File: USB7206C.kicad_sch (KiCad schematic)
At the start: 38 parts, among them J1 USB_SPI_(Opt), SW1 RESET_HUB, U2 MIC803-29D4VM3-TR, U27 USB7206C/KDX, Y1 25MHz

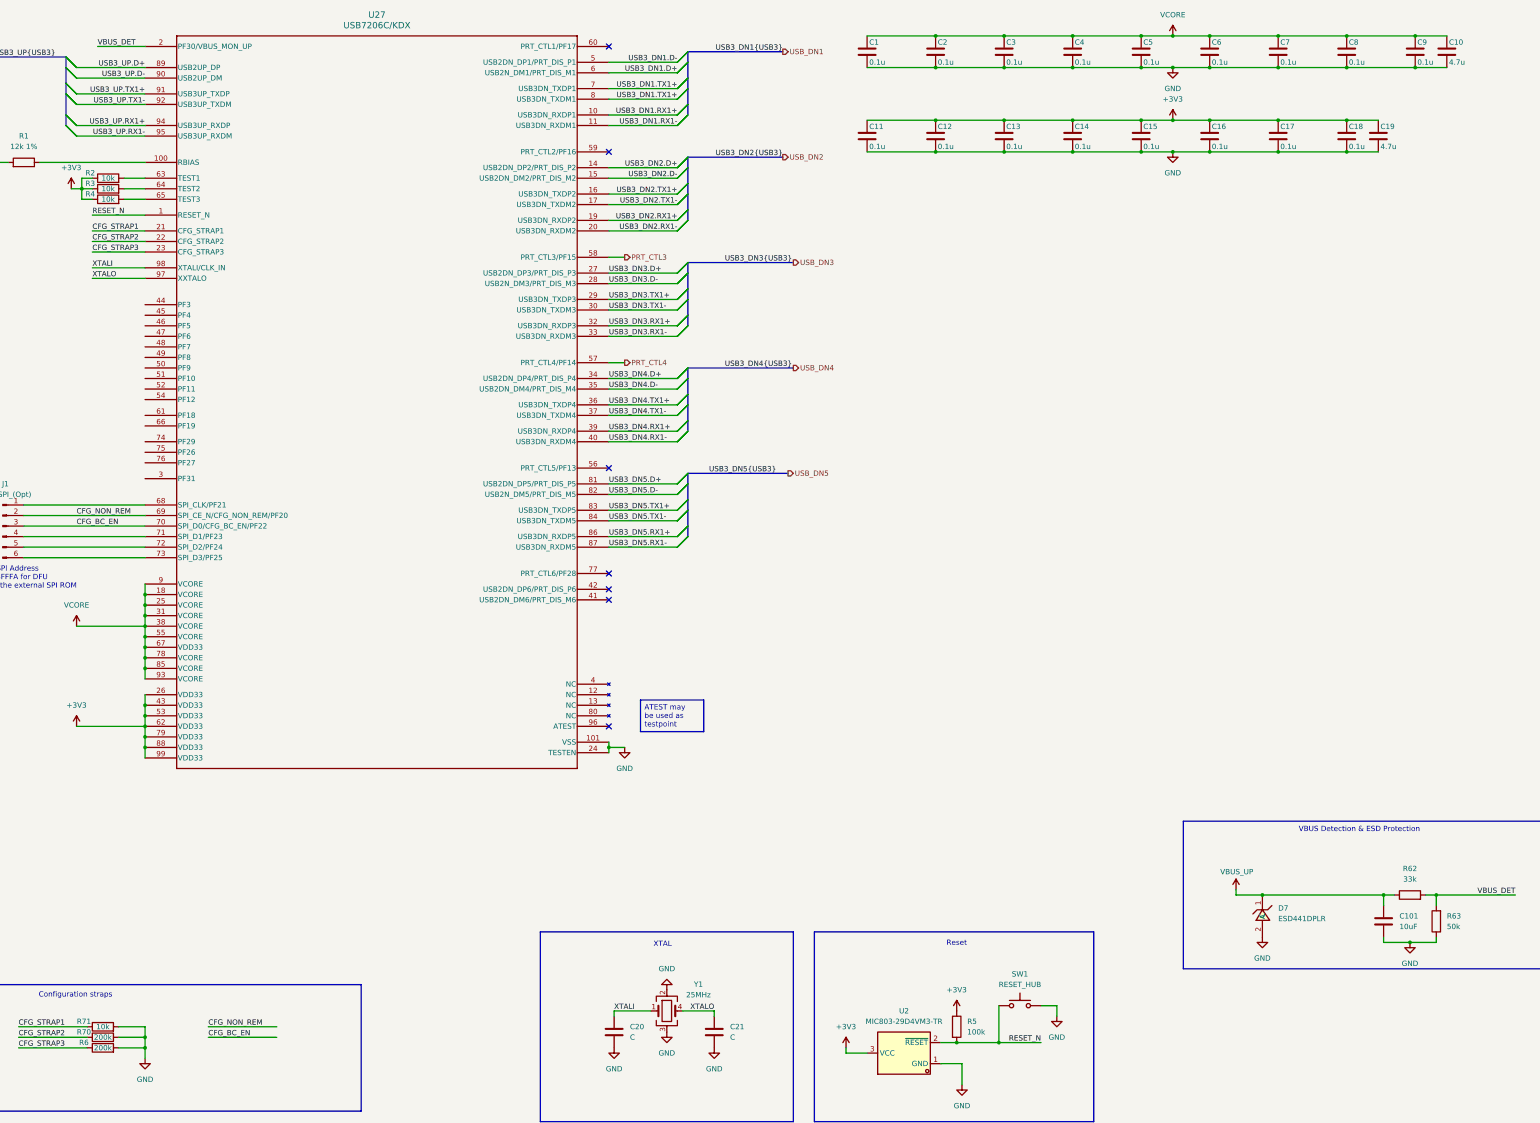
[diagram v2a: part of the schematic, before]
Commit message: Schematic reannotated
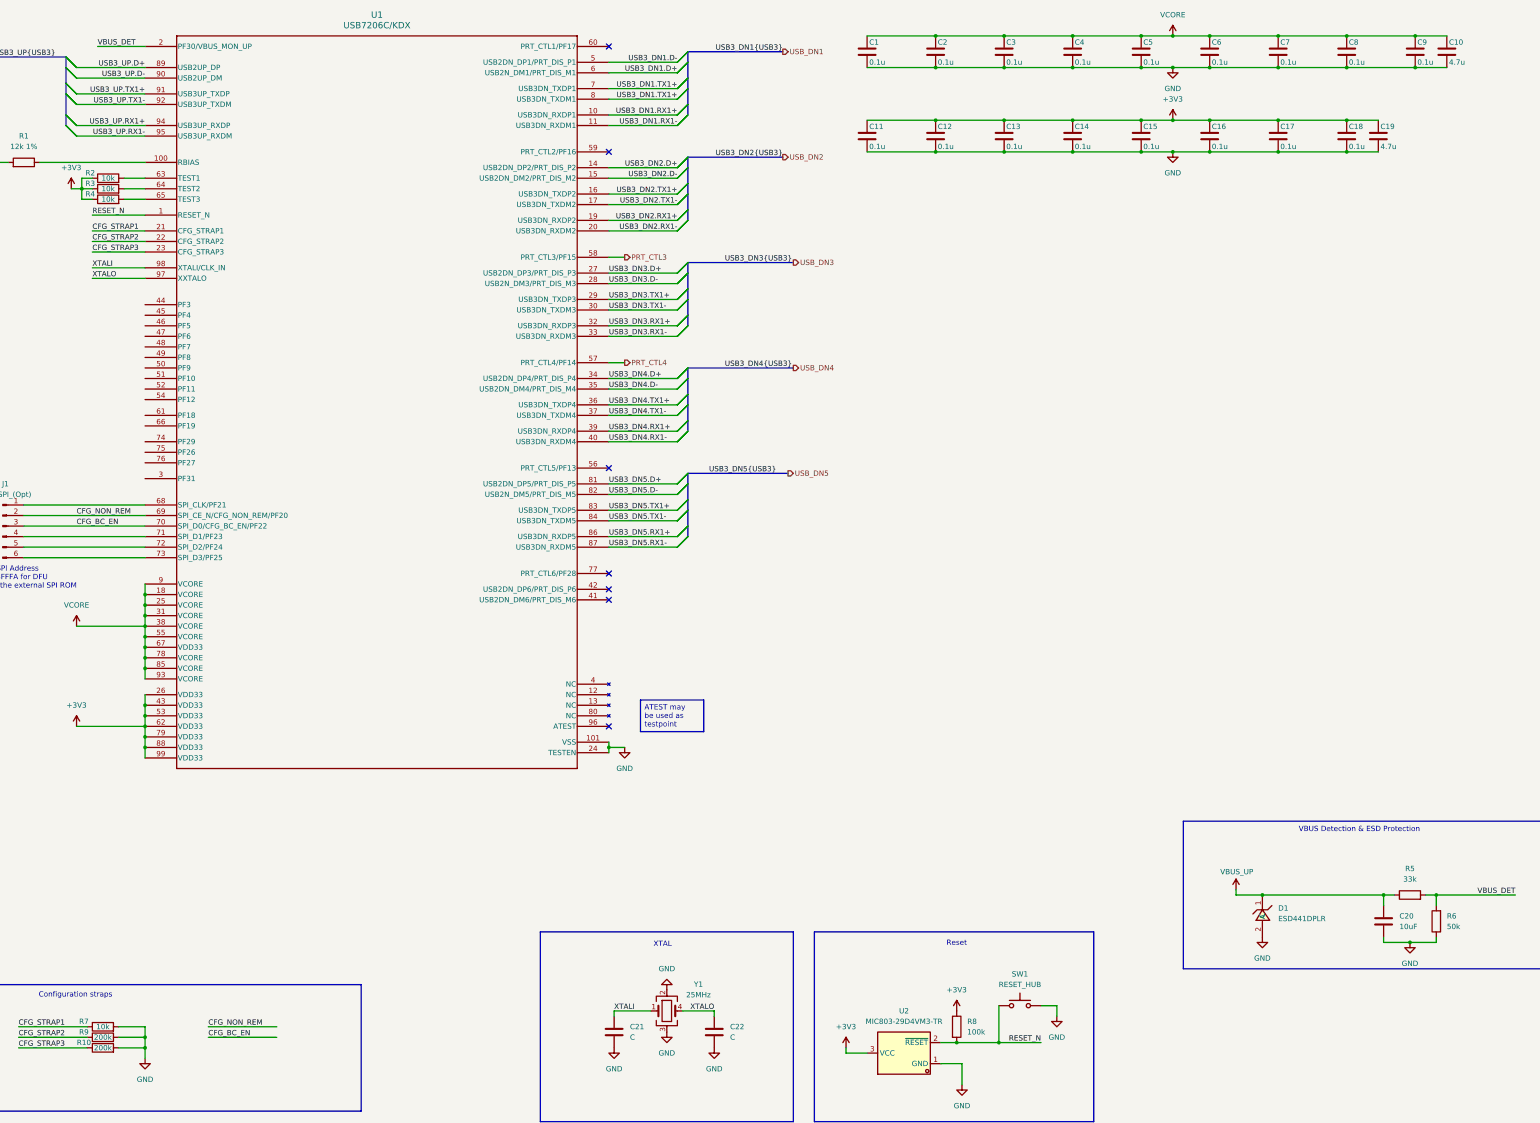
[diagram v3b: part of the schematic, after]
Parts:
- renumbered C101 to C20, C20 to C21, C21 to C22, D7 to D1, R6 to R10, R62 to R5, R63 to R6, R71 to R7, R5 to R8, R70 to R9, U27 to U1
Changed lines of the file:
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@@
 		(on_board yes)
 		(dnp no)
-		(property "Reference" "#PWR0186"
+		(property "Reference" "#PWR010"
 			(at 323.85 229.87 0)
 			(effects
@@
 			(project "USB_hub"
 				(path "/a2586c28-95f1-49e6-9254-37d7a8473e53/84084c93-70ae-4353-a3b8-87defd735fb2"
-					(reference "#PWR0186")
+					(reference "#PWR010")
 					(unit 1)
 				)
@@
 		(dnp no)
 		(fields_autoplaced yes)
-		(property "Reference" "#PWR025"
+		(property "Reference" "#PWR013"
 			(at 186.69 243.84 0)
 			(effects
@@
 			(project "USB_hub"
 				(path "/a2586c28-95f1-49e6-9254-37d7a8473e53/84084c93-70ae-4353-a3b8-87defd735fb2"
-					(reference "#PWR025")
+					(reference "#PWR013")
 					(unit 1)
 				)
@@
 		(dnp no)
 		(fields_autoplaced yes)
-		(property "Reference" "C20"
+		(property "Reference" "C21"
 			(at 177.8 259.0799 0)
 			(effects
@@
 			(project "USB_hub"
 				(path "/a2586c28-95f1-49e6-9254-37d7a8473e53/84084c93-70ae-4353-a3b8-87defd735fb2"
-					(reference "C20")
+					(reference "C21")
 					(unit 1)
 				)
@@
 		(dnp no)
 		(fields_autoplaced yes)
-		(property "Reference" "#PWR026"
+		(property "Reference" "#PWR014"
 			(at 256.54 259.08 0)
 			(effects
@@
 			(project "USB_hub"
 				(path "/a2586c28-95f1-49e6-9254-37d7a8473e53/84084c93-70ae-4353-a3b8-87defd735fb2"
-					(reference "#PWR026")
+					(reference "#PWR014")
 					(unit 1)
 				)
@@
 		(dnp no)
 		(fields_autoplaced yes)
-		(property "Reference" "R62"
+		(property "Reference" "R5"
 			(at 365.76 220.98 90)
 			(effects
@@
 			(project "USB_hub"
 				(path "/a2586c28-95f1-49e6-9254-37d7a8473e53/84084c93-70ae-4353-a3b8-87defd735fb2"
-					(reference "R62")
+					(reference "R5")
 					(unit 1)
 				)
@@
 		(dnp no)
 		(fields_autoplaced yes)
-		(property "Reference" "R5"
+		(property "Reference" "R8"
 			(at 259.08 257.8099 0)
 			(effects
@@
 			(project ""
 				(path "/a2586c28-95f1-49e6-9254-37d7a8473e53/84084c93-70ae-4353-a3b8-87defd735fb2"
-					(reference "R5")
+					(reference "R8")
 					(unit 1)
 				)
@@
 		(dnp no)
 		(fields_autoplaced yes)
-		(property "Reference" "#PWR028"
+		(property "Reference" "#PWR016"
 			(at 186.69 266.7 0)
 			(effects
@@
 			(project "USB_hub"
 				(path "/a2586c28-95f1-49e6-9254-37d7a8473e53/84084c93-70ae-4353-a3b8-87defd735fb2"
-					(reference "#PWR028")
+					(reference "#PWR016")
 					(unit 1)
 				)
@@
 		(on_board yes)
 		(dnp no)
-		(property "Reference" "R71"
+		(property "Reference" "R7"
 			(at 46.228 257.81 90)
 			(effects
@@
 			(project "USB_hub"
 				(path "/a2586c28-95f1-49e6-9254-37d7a8473e53/84084c93-70ae-4353-a3b8-87defd735fb2"
-					(reference "R71")
+					(reference "R7")
 					(unit 1)
 				)
@@
 		(dnp no)
 		(fields_autoplaced yes)
-		(property "Reference" "#PWR032"
+		(property "Reference" "#PWR020"
 			(at 60.96 273.05 0)
 			(effects
@@
 			(project ""
 				(path "/a2586c28-95f1-49e6-9254-37d7a8473e53/84084c93-70ae-4353-a3b8-87defd735fb2"
-					(reference "#PWR032")
+					(reference "#PWR020")
 					(unit 1)
 				)
@@
 		(dnp no)
 		(fields_autoplaced yes)
-		(property "Reference" "#PWR033"
+		(property "Reference" "#PWR021"
 			(at 257.81 279.4 0)
 			(effects
@@
 			(project ""
 				(path "/a2586c28-95f1-49e6-9254-37d7a8473e53/84084c93-70ae-4353-a3b8-87defd735fb2"
-					(reference "#PWR033")
+					(reference "#PWR021")
 					(unit 1)
 				)
@@
 		(dnp no)
 		(fields_autoplaced yes)
-		(property "Reference" "#PWR013"
+		(property "Reference" "#PWR08"
 			(at 44.45 190.5 0)
 			(effects
@@
 			(project ""
 				(path "/a2586c28-95f1-49e6-9254-37d7a8473e53/84084c93-70ae-4353-a3b8-87defd735fb2"
-					(reference "#PWR013")
+					(reference "#PWR08")
 					(unit 1)
 				)
@@
 		(dnp no)
 		(fields_autoplaced yes)
-		(property "Reference" "C21"
+		(property "Reference" "C22"
 			(at 201.93 259.0799 0)
 			(effects
@@
 			(project "USB_hub"
 				(path "/a2586c28-95f1-49e6-9254-37d7a8473e53/84084c93-70ae-4353-a3b8-87defd735fb2"
-					(reference "C21")
+					(reference "C22")
 					(unit 1)
 				)
@@
 		(dnp no)
 		(fields_autoplaced yes)
-		(property "Reference" "#PWR027"
+		(property "Reference" "#PWR015"
 			(at 280.67 262.89 0)
 			(effects
@@
 			(project "USB_hub"
 				(path "/a2586c28-95f1-49e6-9254-37d7a8473e53/84084c93-70ae-4353-a3b8-87defd735fb2"
-					(reference "#PWR027")
+					(reference "#PWR015")
 					(unit 1)
 				)
@@
 		(dnp no)
 		(fields_autoplaced yes)
-		(property "Reference" "#PWR031"
+		(property "Reference" "#PWR019"
 			(at 229.87 267.97 0)
 			(effects
@@
 			(project "USB_hub"
 				(path "/a2586c28-95f1-49e6-9254-37d7a8473e53/84084c93-70ae-4353-a3b8-87defd735fb2"
-					(reference "#PWR031")
+					(reference "#PWR019")
 					(unit 1)
 				)
@@
 		(dnp no)
 		(fields_autoplaced yes)
-		(property "Reference" "#PWR06"
+		(property "Reference" "#PWR04"
 			(at 308.61 54.61 0)
 			(effects
@@
 			(project "USB_hub"
 				(path "/a2586c28-95f1-49e6-9254-37d7a8473e53/84084c93-70ae-4353-a3b8-87defd735fb2"
-					(reference "#PWR06")
+					(reference "#PWR04")
 					(unit 1)
 				)
@@
 		(dnp no)
 		(fields_autoplaced yes)
-		(property "Reference" "#PWR029"
+		(property "Reference" "#PWR017"
 			(at 173.99 270.51 0)
 			(effects
@@
 			(project "USB_hub"
 				(path "/a2586c28-95f1-49e6-9254-37d7a8473e53/84084c93-70ae-4353-a3b8-87defd735fb2"
-					(reference "#PWR029")
+					(reference "#PWR017")
 					(unit 1)
 				)
@@
 		(on_board yes)
 		(dnp no)
-		(property "Reference" "R6"
+		(property "Reference" "R10"
 			(at 46.228 262.89 90)
 			(effects
@@
 			(project ""
 				(path "/a2586c28-95f1-49e6-9254-37d7a8473e53/84084c93-70ae-4353-a3b8-87defd735fb2"
-					(reference "R6")
+					(reference "R10")
 					(unit 1)
 				)
@@
 		(dnp no)
 		(fields_autoplaced yes)
-		(property "Reference" "#PWR04"
+		(property "Reference" "#PWR09"
 			(at 176.53 198.12 0)
 			(effects
@@
 			(project "USB_hub"
 				(path "/a2586c28-95f1-49e6-9254-37d7a8473e53/84084c93-70ae-4353-a3b8-87defd735fb2"
-					(reference "#PWR04")
+					(reference "#PWR09")
 					(unit 1)
 				)
@@
 		(dnp no)
 		(fields_autoplaced yes)
-		(property "Reference" "D7"
+		(property "Reference" "D1"
 			(at 334.01 230.5049 90)
 			(effects
@@
 			(project "USB_hub"
 				(path "/a2586c28-95f1-49e6-9254-37d7a8473e53/84084c93-70ae-4353-a3b8-87defd735fb2"
-					(reference "D7")
+					(reference "D1")
 					(unit 1)
 				)
@@
 		(dnp no)
 		(fields_autoplaced yes)
-		(property "Reference" "#PWR0188"
+		(property "Reference" "#PWR012"
 			(at 365.76 245.11 0)
 			(effects
@@
 			(project "USB_hub"
 				(path "/a2586c28-95f1-49e6-9254-37d7a8473e53/84084c93-70ae-4353-a3b8-87defd735fb2"
-					(reference "#PWR0188")
+					(reference "#PWR012")
 					(unit 1)
 				)
@@
 		(dnp no)
 		(fields_autoplaced yes)
-		(property "Reference" "#PWR0187"
+		(property "Reference" "#PWR011"
 			(at 330.2 243.84 0)
 			(effects
@@
 			(project "USB_hub"
 				(path "/a2586c28-95f1-49e6-9254-37d7a8473e53/84084c93-70ae-4353-a3b8-87defd735fb2"
-					(reference "#PWR0187")
+					(reference "#PWR011")
 					(unit 1)
 				)
@@
 		(dnp no)
 		(fields_autoplaced yes)
-		(property "Reference" "#PWR024"
+		(property "Reference" "#PWR07"
 			(at 44.45 166.37 0)
 			(effects
@@
 			(project "USB_hub"
 				(path "/a2586c28-95f1-49e6-9254-37d7a8473e53/84084c93-70ae-4353-a3b8-87defd735fb2"
-					(reference "#PWR024")
+					(reference "#PWR07")
 					(unit 1)
 				)
@@
 		(dnp no)
 		(fields_autoplaced yes)
-		(property "Reference" "#PWR014"
+		(property "Reference" "#PWR05"
 			(at 22.86 57.15 0)
 			(effects
@@
 			(project ""
 				(path "/a2586c28-95f1-49e6-9254-37d7a8473e53/84084c93-70ae-4353-a3b8-87defd735fb2"
-					(reference "#PWR014")
+					(reference "#PWR05")
 					(unit 1)
 				)
@@
 		(dnp no)
 		(fields_autoplaced yes)
-		(property "Reference" "U27"
+		(property "Reference" "U1"
 			(at 116.84 15.24 0)
 			(effects
@@
 			(project "USB_hub"
 				(path "/a2586c28-95f1-49e6-9254-37d7a8473e53/84084c93-70ae-4353-a3b8-87defd735fb2"
-					(reference "U27")
+					(reference "U1")
 					(unit 1)
 				)
@@
 		(on_board yes)
 		(dnp no)
-		(property "Reference" "R70"
+		(property "Reference" "R9"
 			(at 46.228 260.35 90)
 			(effects
@@
 			(project "USB_hub"
 				(path "/a2586c28-95f1-49e6-9254-37d7a8473e53/84084c93-70ae-4353-a3b8-87defd735fb2"
-					(reference "R70")
+					(reference "R9")
 					(unit 1)
 				)
@@
 		(dnp no)
 		(fields_autoplaced yes)
-		(property "Reference" "#PWR019"
+		(property "Reference" "#PWR06"
 			(at 43.18 60.96 0)
 			(effects
@@
 			(project "USB_hub"
 				(path "/a2586c28-95f1-49e6-9254-37d7a8473e53/84084c93-70ae-4353-a3b8-87defd735fb2"
-					(reference "#PWR019")
+					(reference "#PWR06")
 					(unit 1)
 				)
@@
 		(dnp no)
 		(fields_autoplaced yes)
-		(property "Reference" "#PWR030"
+		(property "Reference" "#PWR018"
 			(at 198.12 270.51 0)
 			(effects
@@
 			(project "USB_hub"
 				(path "/a2586c28-95f1-49e6-9254-37d7a8473e53/84084c93-70ae-4353-a3b8-87defd735fb2"
-					(reference "#PWR030")
+					(reference "#PWR018")
 					(unit 1)
 				)
@@
 		(dnp no)
 		(fields_autoplaced yes)
-		(property "Reference" "C101"
+		(property "Reference" "C20"
 			(at 363.22 232.4099 0)
 			(effects
@@
 			(project "USB_hub"
 				(path "/a2586c28-95f1-49e6-9254-37d7a8473e53/84084c93-70ae-4353-a3b8-87defd735fb2"
-					(reference "C101")
+					(reference "C20")
 					(unit 1)
 				)
@@
 		(dnp no)
 		(fields_autoplaced yes)
-		(property "Reference" "R63"
+		(property "Reference" "R6"
 			(at 374.65 232.4099 0)
 			(effects
@@
 			(project "USB_hub"
 				(path "/a2586c28-95f1-49e6-9254-37d7a8473e53/84084c93-70ae-4353-a3b8-87defd735fb2"
-					(reference "R63")
+					(reference "R6")
 					(unit 1)
 				)

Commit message: J11 changed to 8-pin PCIe connector, footprint assigned
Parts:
- J1: footprint Connector_PinHeader_1.27mm:PinHeader_1x05_P1.27mm_Vertical -> Connector_PinHeader_1.27mm:PinHeader_1x06_P1.27mm_Vertical
- U1: footprint VQFN100_KDX_MCH -> SamacSys_Parts:QFN40P1200X1200X90-101N-D
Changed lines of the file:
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@@
 			)
 		)
-		(property "Footprint" "Connector_PinHeader_1.27mm:PinHeader_1x05_P1.27mm_Vertical"
+		(property "Footprint" "Connector_PinHeader_1.27mm:PinHeader_1x06_P1.27mm_Vertical"
 			(at 26.67 138.43 0)
 			(effects
@@
 			)
 		)
-		(property "Footprint" "VQFN100_KDX_MCH"
+		(property "Footprint" "SamacSys_Parts:QFN40P1200X1200X90-101N-D"
 			(at 60.96 25.4 0)
 			(effects
